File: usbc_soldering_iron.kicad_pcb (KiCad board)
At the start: 2 copper layers, 82 parts, among them J3 USB_C_Receptacle_USB2.0_14P, J6 OLED, Q1 DMP6023LE, Q2 MMBT3904, SW1 RST, SW2 B1, SW3 B2, SW4 B3, SW5 BS, U1 SRV05-4, U2 MCP6001-OT, U3 CH32V203GxUx, U4 AP63201WU, U5 FUSB302BMPX, U6 TLV333IDBVR, U7 SC7A20

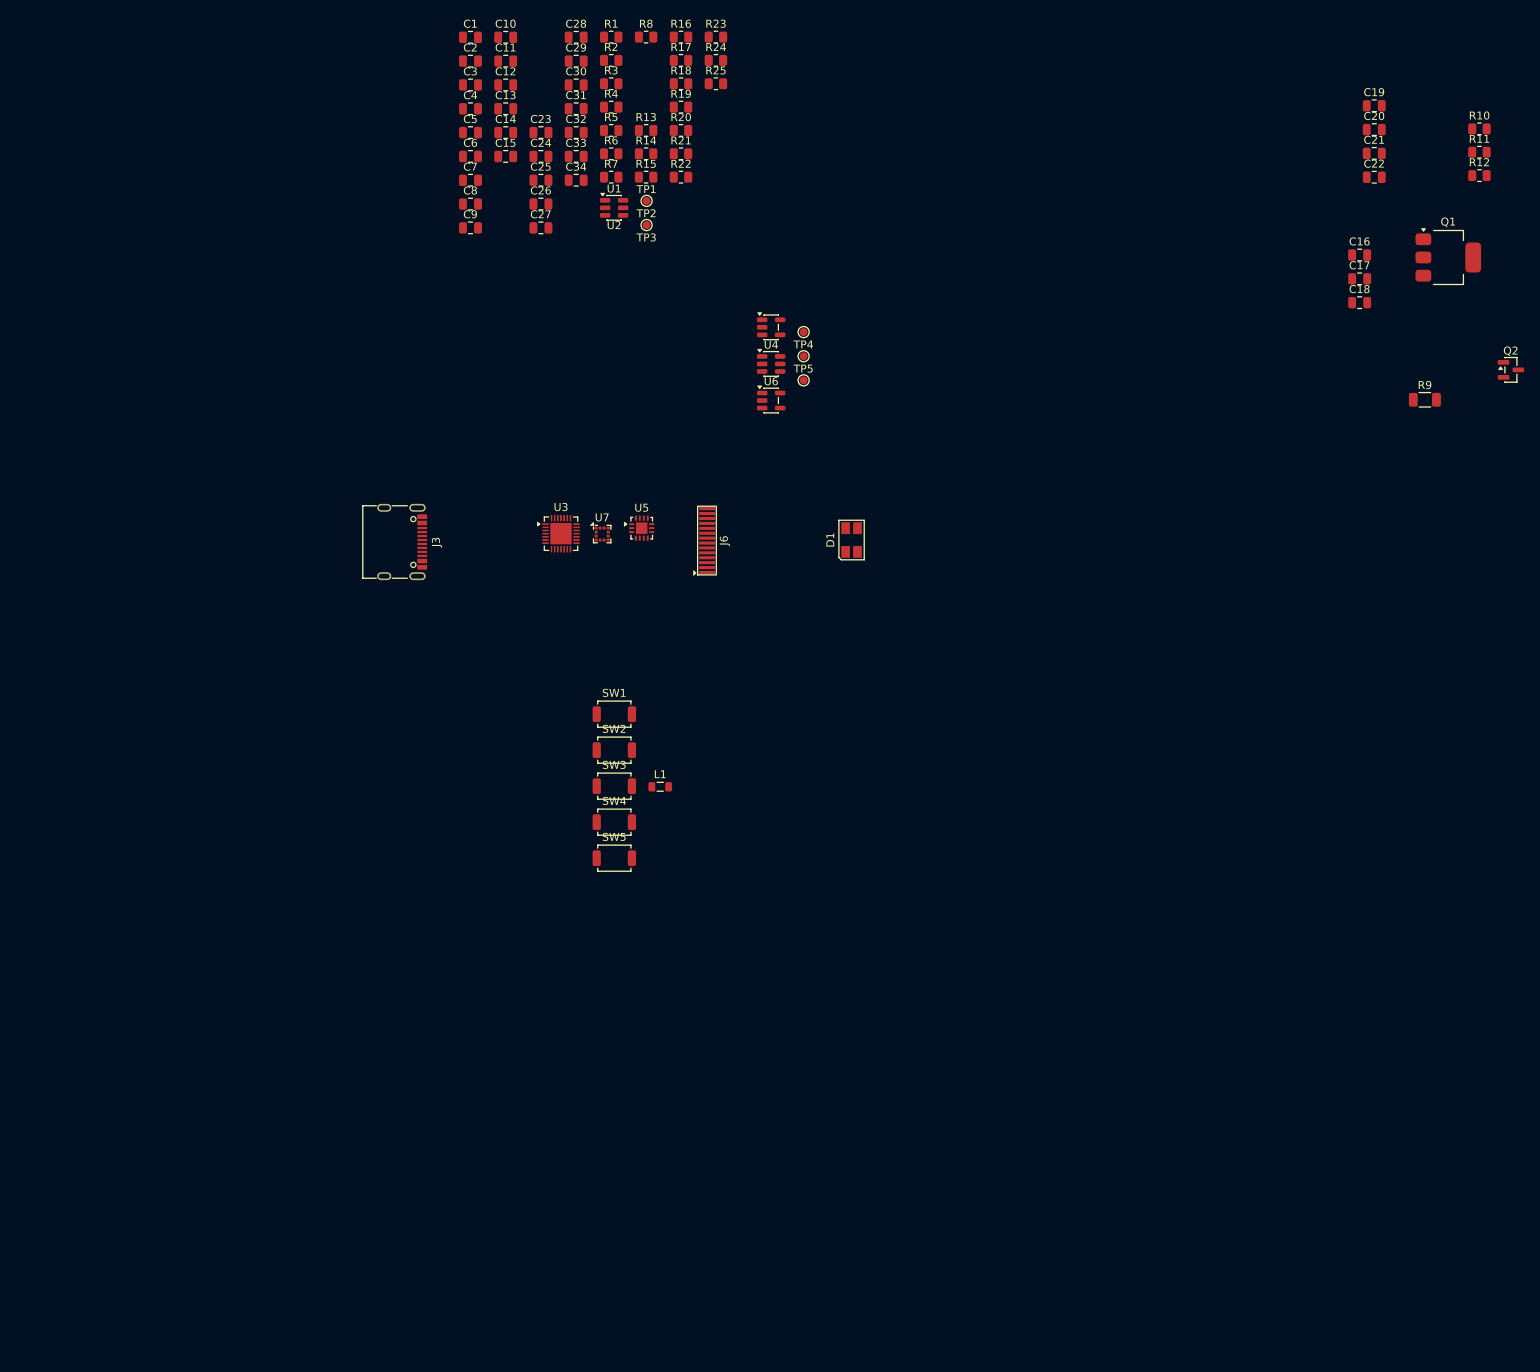
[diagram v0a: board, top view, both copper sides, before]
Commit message: board dimensions and different components
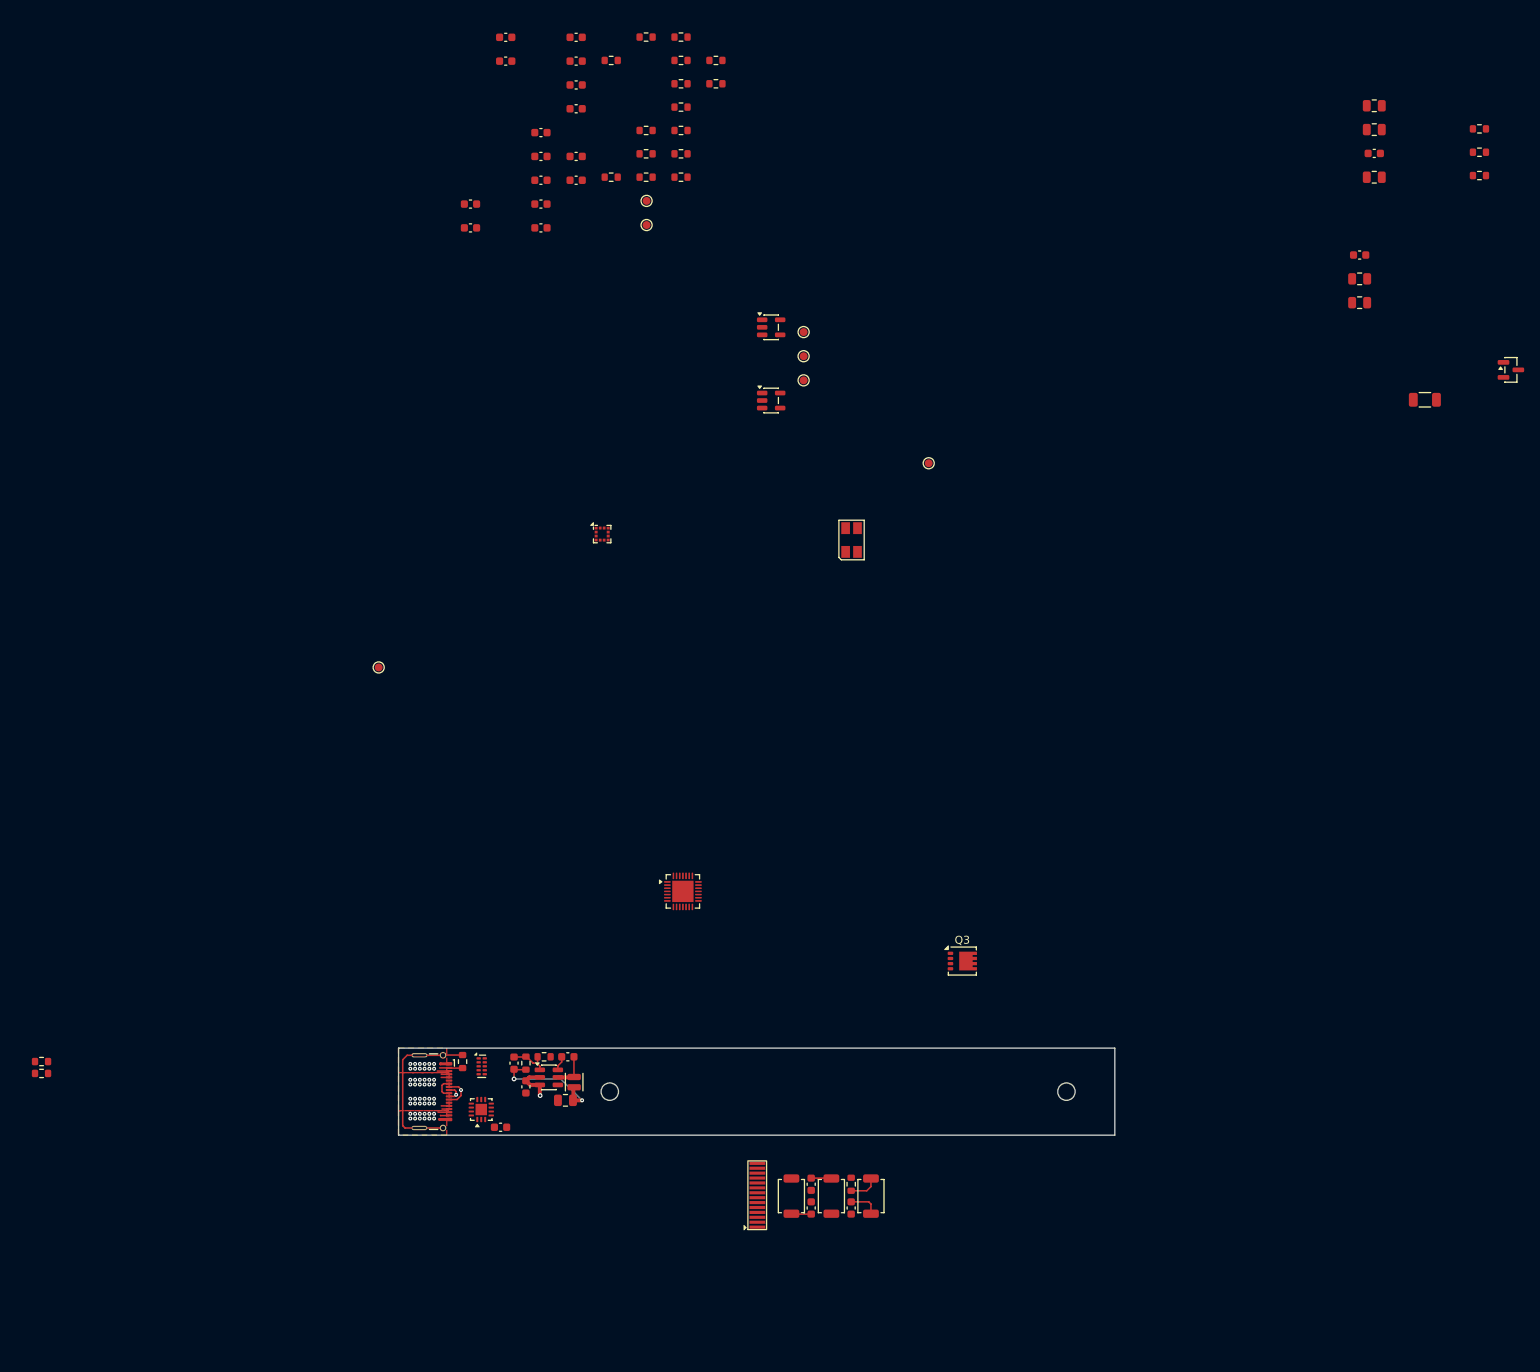
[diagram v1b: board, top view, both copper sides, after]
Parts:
- removed the C1 at (109.6, 19.5)
- removed the C12 at (114.0, 25.5)
- removed the C15 at (114.0, 34.5)
- removed the C5 at (109.6, 31.5)
- removed the Q1 at (233.2, 47.3)
- removed SW1: RST, Button_Switch_SMD:SW_SPST_TS-1088-xR020
- removed the SW4 at (127.8, 118.7)
- removed the U1 at (127.8, 41.0)
- added H1: MountingHole, MountingHole:MountingHole_2.2mm_M2, F.Cu at (127.2, 152.7)
- added H2: MountingHole, MountingHole:MountingHole_2.2mm_M2, F.Cu at (184.9, 152.7)
- added Q3: DMP3013SFV, Package_SON:Diodes_PowerDI3333-8, F.Cu at (171.7, 136.2)
- added TP1: TP_PD1, TestPoint:TestPoint_Pad_D1.0mm, F.Cu at (167.5, 73.3)
- added TP7: TP_PD1, TestPoint:TestPoint_Pad_D1.0mm, F.Cu at (98.0, 99.1)
- added U8: TPD4E05U06DQA, Package_SON:USON-10_2.5x1.0mm_P0.5mm, F.Cu at (111.0, 149.5)
- C1: renamed from C8; footprint Capacitor_SMD:C_0805_2012Metric -> Capacitor_SMD:C_0603_1608Metric
- C10: renamed from C3; footprint Capacitor_SMD:C_0805_2012Metric -> Capacitor_SMD:C_0603_1608Metric
- C11: renamed from C14; footprint Capacitor_SMD:C_0805_2012Metric -> Capacitor_SMD:C_0603_1608Metric
- C12: renamed from C6; footprint Capacitor_SMD:C_0805_2012Metric -> Capacitor_SMD:C_0603_1608Metric
- C13: renamed from C32; footprint Capacitor_SMD:C_0805_2012Metric -> Capacitor_SMD:C_0603_1608Metric
- C15: renamed from C34; footprint Capacitor_SMD:C_0805_2012Metric -> Capacitor_SMD:C_0603_1608Metric
- C16: renamed from C33; footprint Capacitor_SMD:C_0805_2012Metric -> Capacitor_SMD:C_0603_1608Metric
- C17: renamed from C29; footprint Capacitor_SMD:C_0805_2012Metric -> Capacitor_SMD:C_0603_1608Metric
- C18: renamed from C26; footprint Capacitor_SMD:C_0805_2012Metric -> Capacitor_SMD:C_0603_1608Metric
- C19: renamed from C27; footprint Capacitor_SMD:C_0805_2012Metric -> Capacitor_SMD:C_0603_1608Metric
- C2: renamed from C9; footprint Capacitor_SMD:C_0805_2012Metric -> Capacitor_SMD:C_0603_1608Metric
- C20: renamed from C28; footprint Capacitor_SMD:C_0805_2012Metric -> Capacitor_SMD:C_0603_1608Metric
- C21: renamed from C30; footprint Capacitor_SMD:C_0805_2012Metric -> Capacitor_SMD:C_0603_1608Metric
- C22: renamed from C31; footprint Capacitor_SMD:C_0805_2012Metric -> Capacitor_SMD:C_0603_1608Metric
- C23: footprint Capacitor_SMD:C_0805_2012Metric -> Capacitor_SMD:C_0603_1608Metric
- C28: renamed from C24; footprint Capacitor_SMD:C_0805_2012Metric -> Capacitor_SMD:C_0603_1608Metric
- C3: renamed from C7; footprint Capacitor_SMD:C_0805_2012Metric -> Capacitor_SMD:C_0603_1608Metric
- C30: renamed from C16; footprint Capacitor_SMD:C_0805_2012Metric -> Capacitor_SMD:C_0603_1608Metric
- C31: renamed from C25; footprint Capacitor_SMD:C_0805_2012Metric -> Capacitor_SMD:C_0603_1608Metric
- C32: renamed from C21; footprint Capacitor_SMD:C_0805_2012Metric -> Capacitor_SMD:C_0603_1608Metric
- C5: renamed from C11; footprint Capacitor_SMD:C_0805_2012Metric -> Capacitor_SMD:C_0603_1608Metric
- C6: renamed from C10; footprint Capacitor_SMD:C_0805_2012Metric -> Capacitor_SMD:C_0603_1608Metric
- C7: renamed from C2; footprint Capacitor_SMD:C_0805_2012Metric -> Capacitor_SMD:C_0603_1608Metric
- C9: renamed from C13; footprint Capacitor_SMD:C_0805_2012Metric -> Capacitor_SMD:C_0603_1608Metric
- J1: renamed from J3; footprint Connector_USB:USB_C_Receptacle_G-Switch_GT-USB-7010ASV -> Connector_USB:USB_C_Receptacle_G-Switch_GT-USB-7025
- L1: footprint Inductor_SMD:L_0805_2012Metric -> Inductor_SMD:L_Changjiang_FTC201607S
- R1: footprint Resistor_SMD:R_0805_2012Metric -> Resistor_SMD:R_0603_1608Metric
- R10: renamed from R22; footprint Resistor_SMD:R_0805_2012Metric -> Resistor_SMD:R_0603_1608Metric
- R11: renamed from R3; footprint Resistor_SMD:R_0805_2012Metric -> Resistor_SMD:R_0603_1608Metric
- R12: renamed from R4; footprint Resistor_SMD:R_0805_2012Metric -> Resistor_SMD:R_0603_1608Metric
- R13: renamed from R23; footprint Resistor_SMD:R_0805_2012Metric -> Resistor_SMD:R_0603_1608Metric
- R14: renamed from R21; footprint Resistor_SMD:R_0805_2012Metric -> Resistor_SMD:R_0603_1608Metric
- R15: renamed from R13; footprint Resistor_SMD:R_0805_2012Metric -> Resistor_SMD:R_0603_1608Metric
- R16: renamed from R14; footprint Resistor_SMD:R_0805_2012Metric -> Resistor_SMD:R_0603_1608Metric
- R17: renamed from R15; footprint Resistor_SMD:R_0805_2012Metric -> Resistor_SMD:R_0603_1608Metric
- R18: renamed from R16; footprint Resistor_SMD:R_0805_2012Metric -> Resistor_SMD:R_0603_1608Metric
- R19: renamed from R12; footprint Resistor_SMD:R_0805_2012Metric -> Resistor_SMD:R_0603_1608Metric
- R2: renamed from R5; footprint Resistor_SMD:R_0805_2012Metric -> Resistor_SMD:R_0603_1608Metric
- R20: renamed from R11; footprint Resistor_SMD:R_0805_2012Metric -> Resistor_SMD:R_0603_1608Metric
- R21: renamed from R10; footprint Resistor_SMD:R_0805_2012Metric -> Resistor_SMD:R_0603_1608Metric
- R22: renamed from R19; footprint Resistor_SMD:R_0805_2012Metric -> Resistor_SMD:R_0603_1608Metric
- R23: renamed from R20; footprint Resistor_SMD:R_0805_2012Metric -> Resistor_SMD:R_0603_1608Metric
- R25: renamed from R17; footprint Resistor_SMD:R_0805_2012Metric -> Resistor_SMD:R_0603_1608Metric
- R3: renamed from R6; footprint Resistor_SMD:R_0805_2012Metric -> Resistor_SMD:R_0603_1608Metric
- R4: renamed from R8; footprint Resistor_SMD:R_0805_2012Metric -> Resistor_SMD:R_0603_1608Metric
- R5: renamed from R7; footprint Resistor_SMD:R_0805_2012Metric -> Resistor_SMD:R_0603_1608Metric
- R6: renamed from R2; footprint Resistor_SMD:R_0805_2012Metric -> Resistor_SMD:R_0603_1608Metric
- R7: renamed from R24; footprint Resistor_SMD:R_0805_2012Metric -> Resistor_SMD:R_0603_1608Metric
- R8: renamed from R25; footprint Resistor_SMD:R_0805_2012Metric -> Resistor_SMD:R_0603_1608Metric
- R9: renamed from R18; footprint Resistor_SMD:R_0805_2012Metric -> Resistor_SMD:R_0603_1608Metric
- moved R13 146.0 mm to (157.7, 164.4), turned to -90 degrees
- moved C9 144.2 mm to (152.7, 167.4), turned to 90 degrees
- moved C13 140.3 mm to (157.7, 167.4), turned to -90 degrees
- moved R2 139.2 mm to (55.4, 150.4)
- moved C11 138.4 mm to (152.7, 164.4), turned to -90 degrees
- moved R3 135.4 mm to (55.4, 148.9)
- moved R1 130.8 mm to (108.6, 148.9), turned to -90 degrees
- moved C7 129.8 mm to (116.6, 152.1), turned to -90 degrees
- moved C14 125.9 mm to (121.6, 153.8), turned to 180 degrees
- moved R11 124.2 mm to (116.6, 149.1), turned to 90 degrees
- moved C10 123.4 mm to (121.9, 148.3), turned to 180 degrees
- moved R12 120.3 mm to (118.9, 148.3)
- moved C3 119.7 mm to (113.4, 157.2)
- moved C12 114.7 mm to (115.1, 149.1), turned to 90 degrees
- moved U4 94.4 mm to (119.5, 150.9)
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- renumbered C4 to C14, C22 to C24, C20 to C25, C19 to C26, C18 to C27, C17 to C29, J6 to J4, Q2 to Q1, R9 to R24, SW5 to SW4, TP1 to TP2, TP2 to TP3, TP3 to TP4, TP4 to TP5, TP5 to TP6, U3 to U1, U5 to U2, U7 to U5, U2 to U6, U6 to U7
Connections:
- net Net-(J3-D+-PadA6) renamed /JDP
- net Net-(J3-D--PadA7) renamed /JDN
- U1 pad 24: /BTN3 -> /PB3
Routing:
- net Net-(J1-SHIELD): track 0.00 -> 21.4 mm
- net +3.3V: track 0.00 -> 15.3 mm, vias 0 -> 2
- net GND: track 0.00 -> 9.19 mm, vias 0 -> 24
- net VBUS: track 0.00 -> 9.14 mm, vias 0 -> 25
- net Net-(U4-FB): track 0.00 -> 5.05 mm
- net Net-(U4-SW): track 0.00 -> 4.64 mm
- net /JDP: track 0.00 -> 4.15 mm, vias 0 -> 1
- net /BOOTSEL: track 0.00 -> 3.84 mm
- net Net-(R13-Pad2): track 0.00 -> 3.74 mm
- net (no net): track 0.00 -> 2.74 mm
- net /BTN2: track 0.00 -> 2.57 mm
- net /BTN1: track 0.00 -> 2.52 mm
- net /JDN: track 0.00 -> 2.39 mm, vias 0 -> 1
- net Net-(U4-BST): track 0.00 -> 1.85 mm
- added copper zone on F.Cu, net GND
- added copper zone on In2.Cu, net GND
- added copper zone on F.Cu, net VBUS
- added copper zone on In1.Cu, net VBUS
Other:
- board outline added: 90.5 x 11 mm
- copper layers 2 -> 4

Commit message: some things needed to be 0805
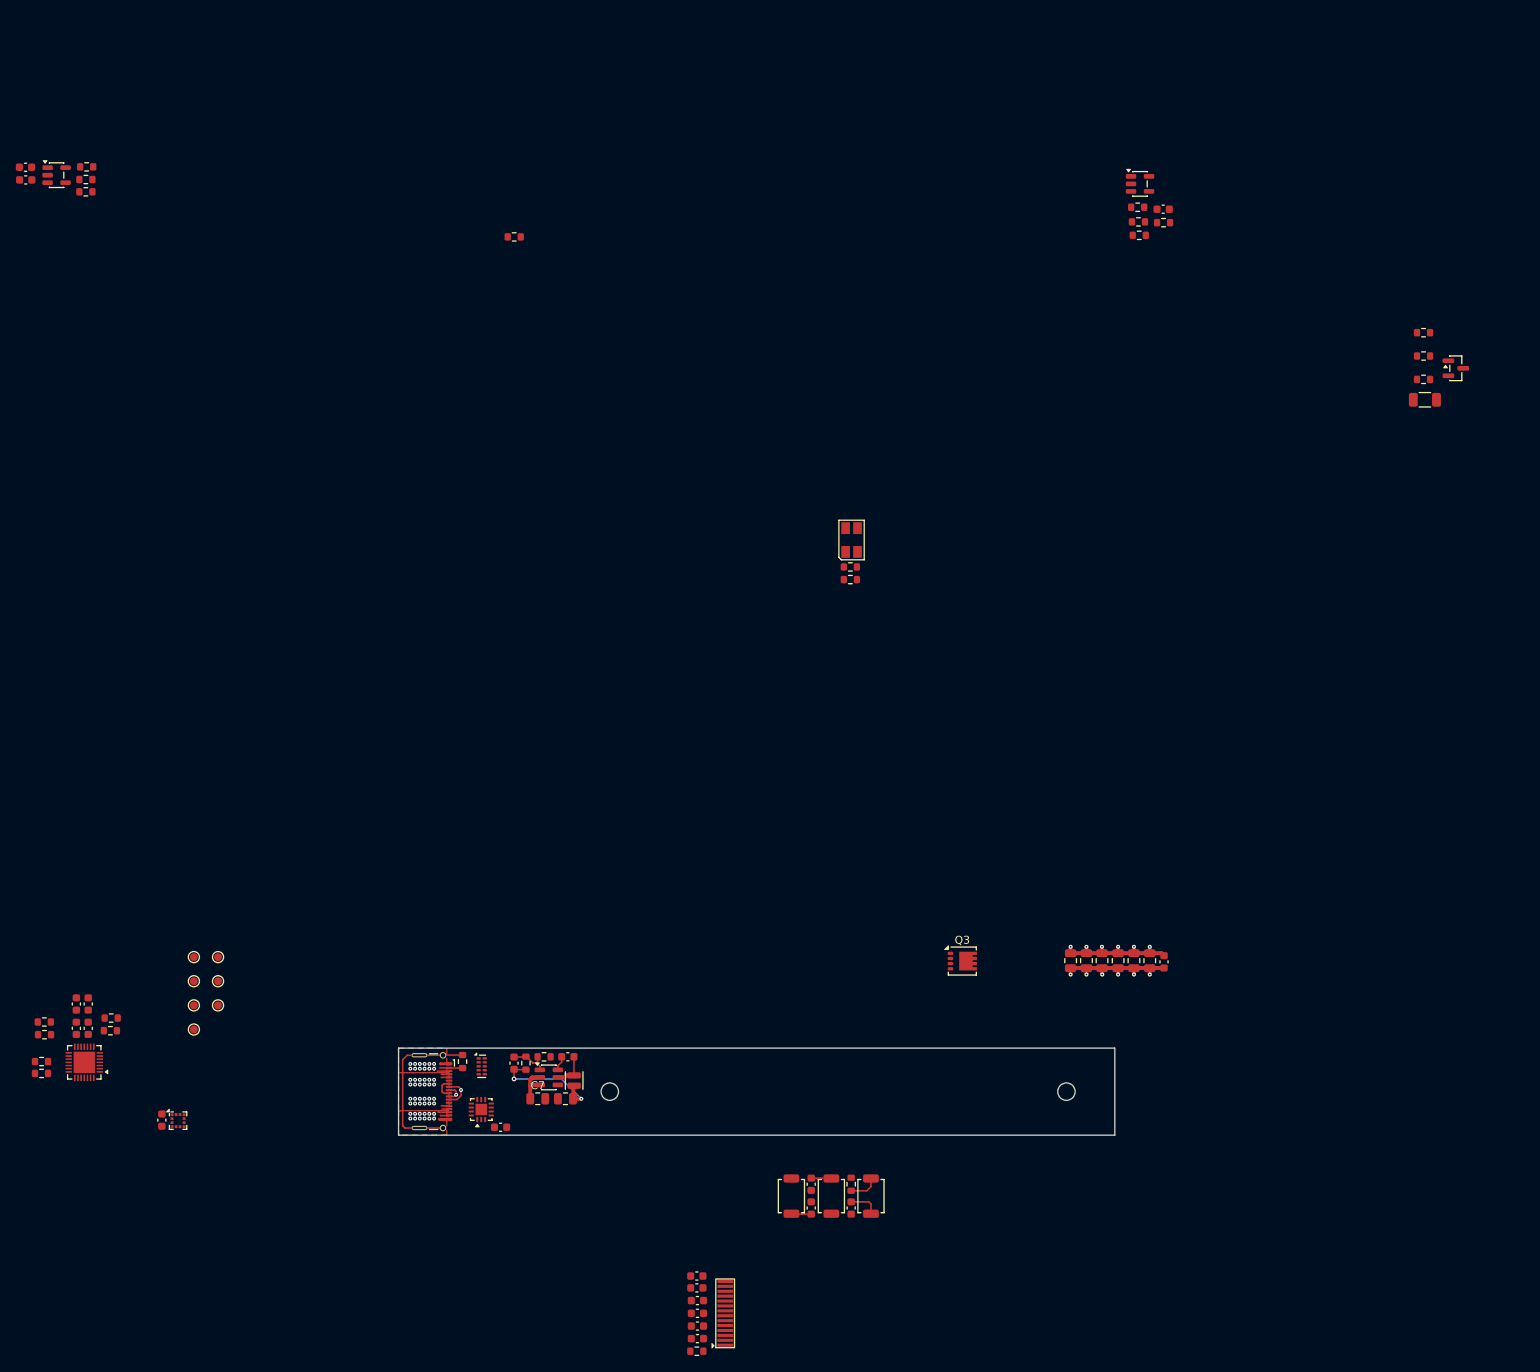
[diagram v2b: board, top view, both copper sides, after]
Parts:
- removed C15: 100n, Capacitor_SMD:C_0603_1608Metric
- C30, C7: footprint Capacitor_SMD:C_0603_1608Metric -> Capacitor_SMD:C_0805_2012Metric
- moved C20 160.4 mm to (138.3, 179.1)
- moved C17 159.0 mm to (138.3, 180.7)
- moved C21 157.6 mm to (138.3, 182.3)
- moved C22 156.2 mm to (138.3, 183.9)
- moved R14 151.3 mm to (138.2, 185.5)
- moved R9 143.3 mm to (55.8, 143.9)
- moved R4 141.2 mm to (64.2, 143.4)
- moved C18 136.9 mm to (138.2, 176.0)
- moved C6 136.5 mm to (59.8, 144.7), turned to 90 degrees
- moved C19 135.4 mm to (138.2, 177.5)
- moved R10 134.9 mm to (55.8, 145.5)
- moved C5 133.1 mm to (61.3, 144.7), turned to 90 degrees
- moved C16 132.5 mm to (70.6, 156.3), turned to 90 degrees
- moved R5 125.0 mm to (64.1, 145.0)
- moved TP4 117.1 mm to (74.7, 144.8)
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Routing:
- net GND: track 9.19 -> 25.8 mm, vias 24 -> 30
- net VBUS: track 9.14 -> 25.6 mm, vias 25 -> 30
